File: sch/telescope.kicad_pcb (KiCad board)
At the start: 2 copper layers, 56.2 x 77 mm, 72 parts, among them J1 USB_B, J2 M1, J3 M2, J4 12V, J5 UART, Q1 MMBT3904, Q2 MMBT3904, Q3 MMBT3904, SW1 RST, SW2 IO0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

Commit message: fix feedback resistor value
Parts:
- removed REF**: Ade, Logo:Ade
- R25: value 33k2 -> 10k

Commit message: fix missing copper layer logo
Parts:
- added REF**: Ade, Logo:Ade, F.Cu at (224.5, 100.6)

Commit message: add series resistor to led bjt
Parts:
- added R16: 10k, Resistor_SMD:R_0805_2012Metric_Pad1.20x1.40mm_HandSolder, F.Cu at (225.9, 111.5)
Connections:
- Q1 pad 1: /LED -> Net-(Q1-B)
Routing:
- net Net-(Q1-B): track 0.00 -> 3.64 mm
- net /LED: track 24.7 -> 25.7 mm

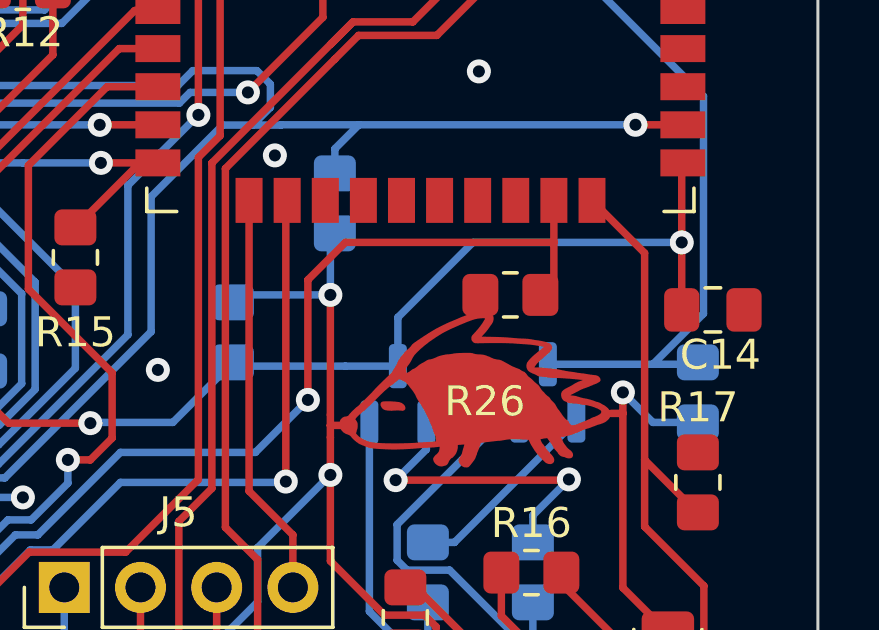
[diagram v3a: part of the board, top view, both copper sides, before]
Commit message: pull down bootstrap pin for serial logging
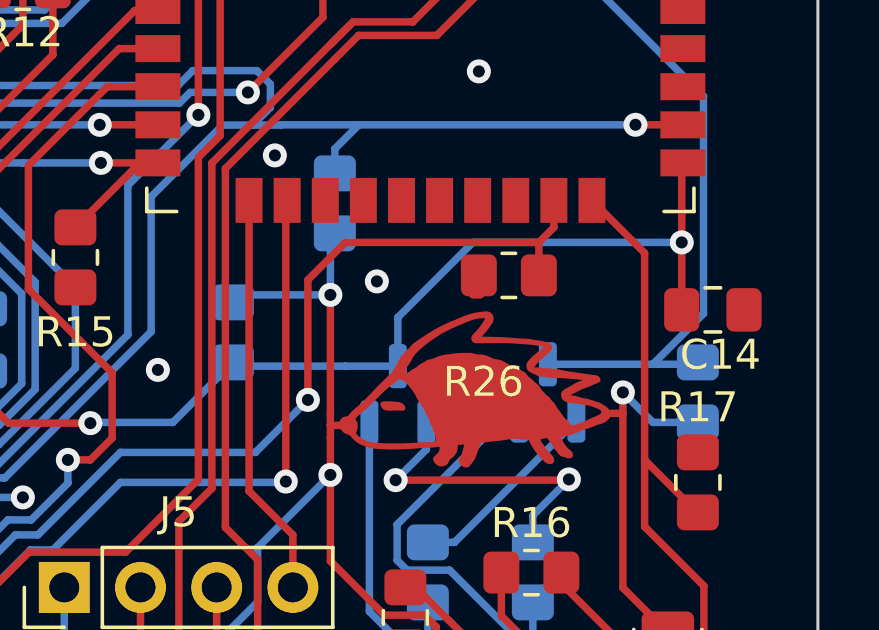
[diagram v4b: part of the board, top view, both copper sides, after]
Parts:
- C13: value 0.1uF -> 1uF
- moved R26 0.65 mm to (225.2, 101.6)
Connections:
- R26 pad 1: +3V3 -> GND
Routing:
- net /M2_STEP: track 35.6 -> 34.4 mm
- net GND: track 31.6 -> 31.9 mm, vias 29 -> 30
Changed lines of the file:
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@@
 	(footprint "Resistor_SMD:R_0805_2012Metric_Pad1.20x1.40mm_HandSolder"
 		(layer "F.Cu")
-		(at 225.25 102.25)
+		(at 225.2 101.6)
 		(descr "Resistor SMD 0805 (2012 Metric), square (rectangular) end terminal, IPC_7351 nominal with elongated pad for handsoldering. (Body size source: IPC-SM-782 page 72, https://www.pcb-3d.com/wordpress/wp-content/uploads/ipc-sm-782a_amendment_1_and_2.pdf), generated with kicad-footprint-generator")
 		(tags "resistor handsolder")
@@
 			(layers "F.Cu" "F.Paste" "F.Mask")
 			(roundrect_rratio 0.2083333333)
-			(net 9 "+3V3")
+			(net 2 "GND")
 			(pintype "passive")
 		)
@@
 			)
 		)
-		(property "Value" "0.1uF"
+		(property "Value" "1uF"
 			(at 0 -1.68 90)
 			(layer "B.Fab")
@@
 	)
 	(segment
+		(start 224.25 102.25)
+		(end 224 102.25)
+		(width 0.25)
+		(layer "F.Cu")
+		(net 2)
+	)
+	(segment
 		(start 217.775 123.449695)
 		(end 220.112348 121.112348)
@@
 	)
 	(via
+		(at 220.8 101.8)
+		(size 0.8)
+		(drill 0.4)
+		(layers "F.Cu" "B.Cu")
+		(free yes)
+		(net 2)
+	)
+	(via
 		(at 196.75 88)
 		(size 0.8)
@@
 	)
 	(segment
-		(start 224.25 102.25)
-		(end 224 102.25)
-		(width 0.25)
-		(layer "F.Cu")
-		(net 9)
-	)
-	(segment
 		(start 213.9929 127.24993)
 		(end 213.9929 125.949958)
@@
 	)
 	(segment
-		(start 226.7 100.5)
-		(end 226.7 101.8)
+		(start 226.2 100.5)
+		(end 219.75 100.5)
 		(width 0.25)
 		(layer "F.Cu")
@@
 	)
 	(segment
-		(start 226.7 99.1)
-		(end 226.7 100.5)
+		(start 226.2 101.6)
+		(end 226.2 100.5)
 		(width 0.25)
 		(layer "F.Cu")
@@
 	)
 	(segment
-		(start 226.7 100.5)
-		(end 219.75 100.5)
+		(start 226.7 100)
+		(end 226.2 100.5)
 		(width 0.25)
 		(layer "F.Cu")
@@
 	)
 	(segment
-		(start 226.7 101.8)
-		(end 226.25 102.25)
+		(start 226.7 99.1)
+		(end 226.7 100)
 		(width 0.25)
 		(layer "F.Cu")

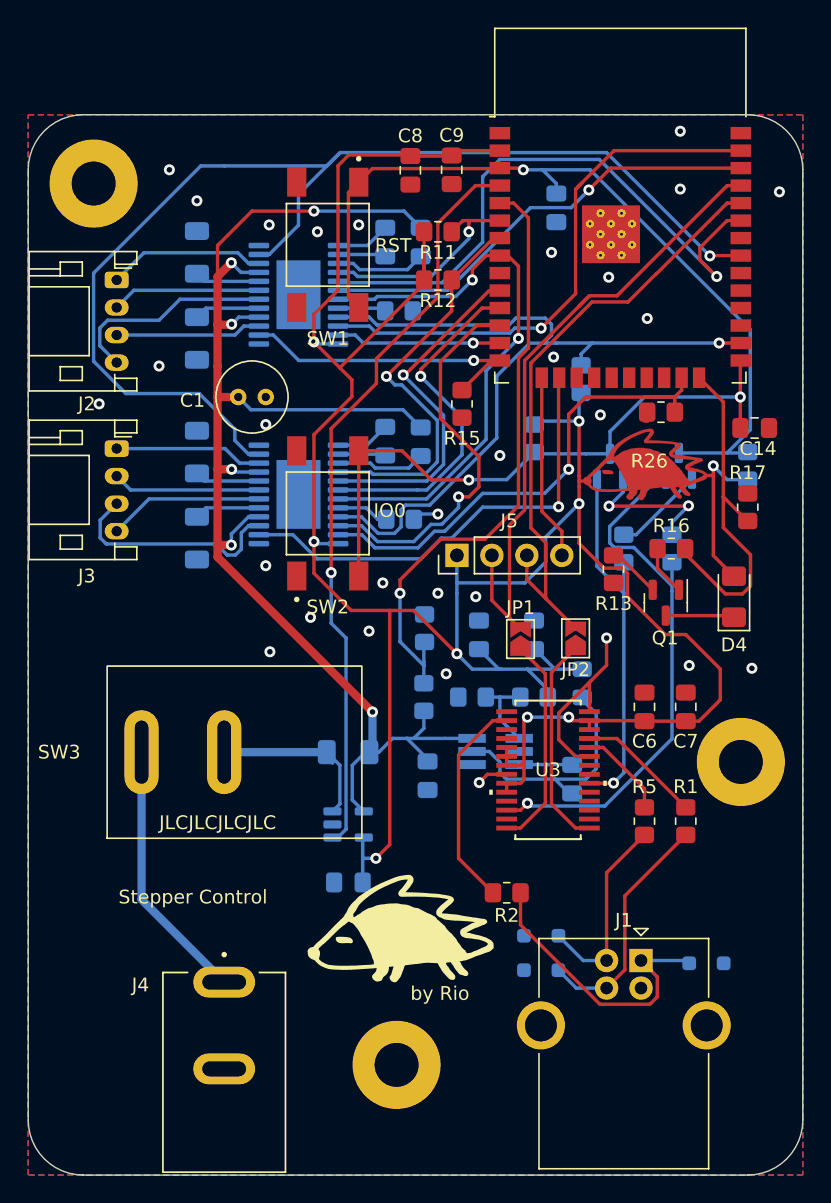
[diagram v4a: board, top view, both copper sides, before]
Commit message: split motor driver enable lines and increase motor trace width
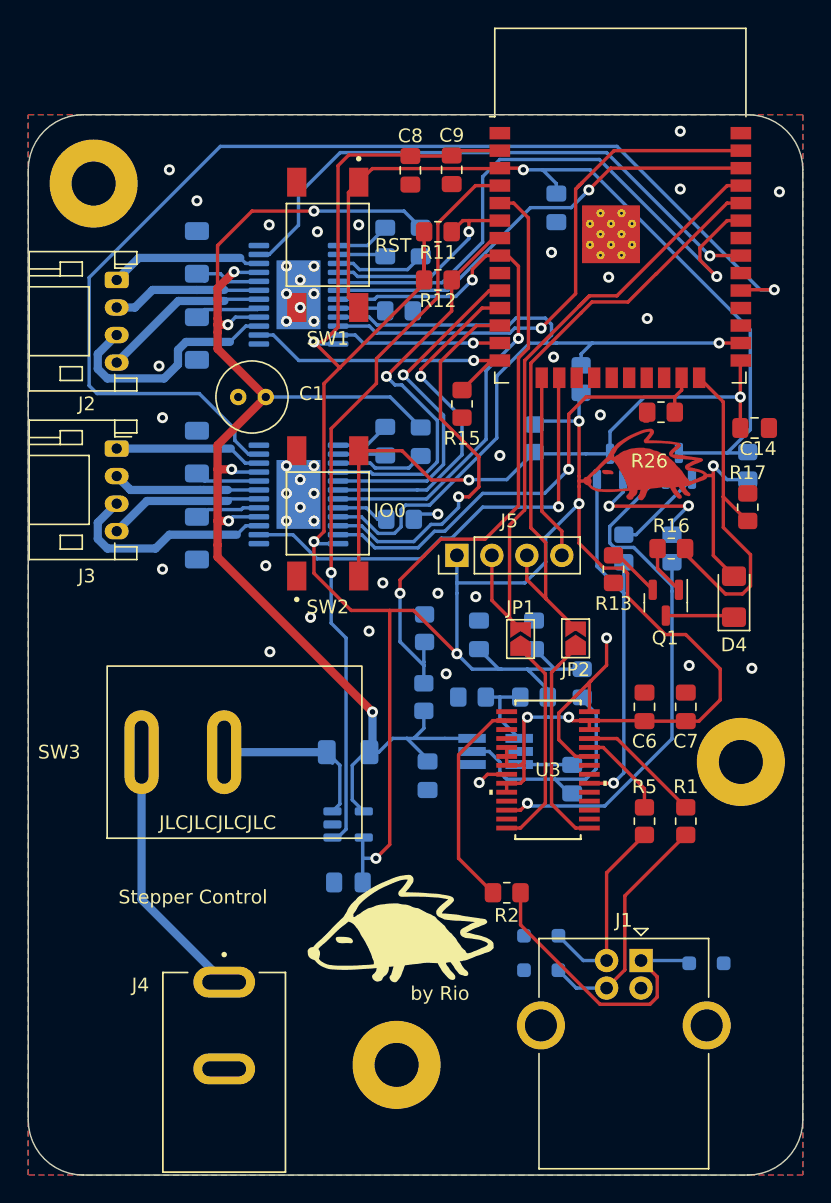
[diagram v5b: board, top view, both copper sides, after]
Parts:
- moved C1 2.00 mm to (196.5, 100.5), turned to 180 degrees
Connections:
- U1 pad 23: /~{M_ENA} -> /~{M1_ENA}
- U2 pad 23: /~{M_ENA} -> /~{M2_ENA}
- U5 pad 29: unconnected-(U5-IO5-Pad29) -> /~{M2_ENA}
- U5 pad 31: /~{M_ENA} -> /~{M1_ENA}
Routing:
- net /~{M_ENA}: track 85.7 -> 0.00 mm, vias 1 -> 0
- net /~{M2_ENA}: track 0.00 -> 83.2 mm, vias 0 -> 1
- net /~{M1_ENA}: track 0.00 -> 42.5 mm, vias 0 -> 1
- net Net-(J2-Pin_3): track 10.6 -> 17.2 mm
- net Net-(J2-Pin_4): track 15.4 -> 12.2 mm
- net +12V: track 106.1 -> 104.1 mm
- net Net-(U1-SENSE2): track 4.73 -> 5.53 mm
- net Net-(J3-Pin_3): track 16.6 -> 15.8 mm
- net GND: vias 30 -> 46

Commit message: update pcb
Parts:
- added D5: PDZ3.6B, Diode_SMD:D_SOD-323_HandSoldering, B.Cu at (219.2, 116.8)
- added D6: CUS10S30, Diode_SMD:D_SOD-323_HandSoldering, F.Cu at (195.2, 139.0)
- added J6: Conn_01x02, Connector_PinHeader_2.54mm:PinHeader_1x02_P2.54mm_Vertical, F.Cu at (207.5, 121.0)
- added JP3: SolderJumper_2_Open, Jumper:SolderJumper-2_P1.3mm_Open_TrianglePad1.0x1.5mm, B.Cu at (203.7, 122.8)
- added JP4: SolderJumper_2_Open, Jumper:SolderJumper-2_P1.3mm_Open_TrianglePad1.0x1.5mm, B.Cu at (203.7, 120.2)
- added Q4: MMBT3904, Package_TO_SOT_SMD:SOT-23, B.Cu at (197.0, 121.0)
- added R27: DNP, Resistor_SMD:R_0805_2012Metric_Pad1.20x1.40mm_HandSolder, F.Cu at (227.4, 101.6)
- added R30: 10k, Resistor_SMD:R_0805_2012Metric_Pad1.20x1.40mm_HandSolder, B.Cu at (198.0, 124.2)
- added RV1: R_Potentiometer_US, Potentiometer_SMD:Potentiometer_Bourns_TC33X_Vertical, B.Cu at (191.0, 118.2)
- added TP1: TestPoint, TestPoint:TestPoint_Pad_D1.5mm, B.Cu at (185.2, 118.2)
- moved R22 9.58 mm to (202.4, 114.5), turned to 180 degrees
- moved R21 5.63 mm to (202.4, 117.2), turned to 0 degrees
- moved R2 4.61 mm to (210.5, 133.5), turned to 90 degrees
- moved R26 1.60 mm to (223.6, 101.6)
- moved C13 1.10 mm to (216.5, 86.8)
- turned C8 to 90 degrees
- turned C9 to 90 degrees
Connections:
- U1 pad 12: +3V3 -> Net-(U1-VREF)
- U2 pad 12: +3V3 -> Net-(U1-VREF)
- U5 pad 27: /GPS_TX -> /GPO
- U5 pad 28: /GPS_RX -> unconnected-(U5-IO17-Pad28)
- U5 pad 30: /GPS_FIX -> unconnected-(U5-IO18-Pad30)
- U5 pad 9: /~{GPS_RST} -> unconnected-(U5-IO33-Pad9)
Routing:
- net /GPO: track 0.00 -> 70.7 mm, vias 0 -> 3
- net Net-(U1-VREF): track 0.00 -> 39.7 mm, vias 0 -> 3
- net VBUS: track 21.6 -> 56.9 mm
- net Net-(J6-Pin_2): track 0.00 -> 10.6 mm, vias 0 -> 1
- net +12V: track 104.1 -> 114.3 mm, vias 6 -> 7
- net /ISENSE: track 54.5 -> 64.7 mm
- net +3V3: track 203.2 -> 212.9 mm
- net Net-(J6-Pin_1): track 0.00 -> 5.42 mm
- net Net-(U3-VBUS_DET): track 15.6 -> 10.5 mm
- net /ESP_EN: track 60.2 -> 65.1 mm, vias 1 -> 3
- net Net-(D6-K): track 19.2 -> 23.4 mm
- net /~{M2_ENA}: track 83.2 -> 86.3 mm
- net /~{M1_ENA}: track 42.5 -> 45.6 mm
- net Net-(Q4-B): track 0.00 -> 2.69 mm
- net GND: track 31.9 -> 34.1 mm, vias 46 -> 49
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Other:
- board text added: "Stepper Control v2"
- board text removed: "JLCJLCJLCJLC"
- board text removed: "Stepper Control"

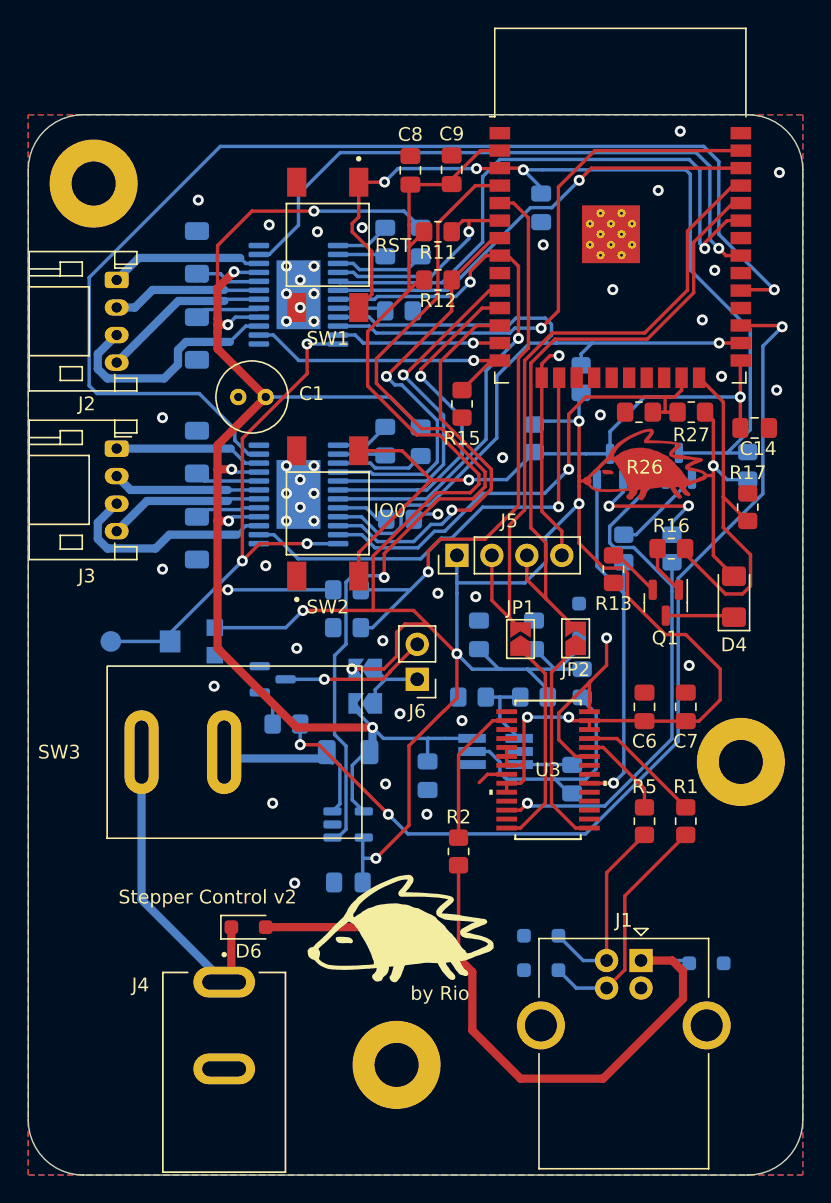
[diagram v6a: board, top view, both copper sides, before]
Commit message: switch to jst and generate v2 gerbers
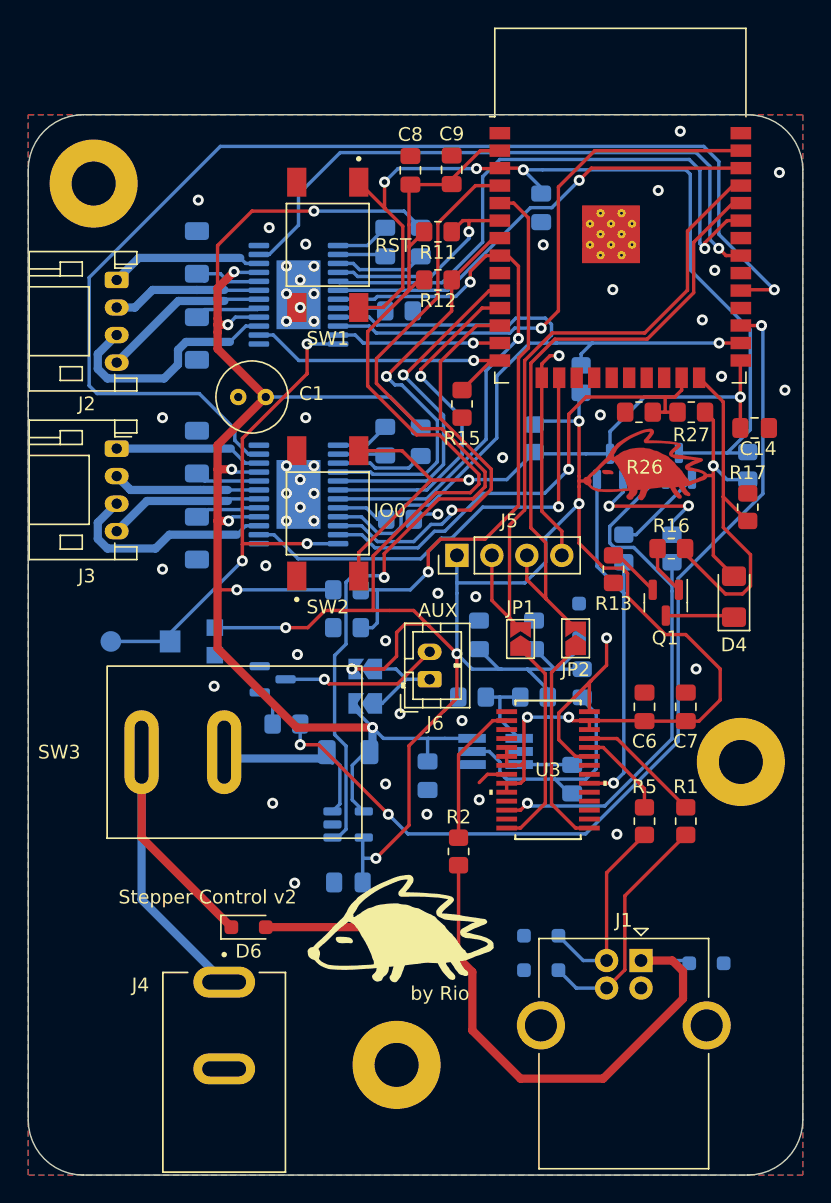
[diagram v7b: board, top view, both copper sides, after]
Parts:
- J6: value Conn_01x02 -> AUX; footprint Connector_PinHeader_2.54mm:PinHeader_1x02_P2.54mm_Vertical -> Connector_JST:JST_PH_B2B-PH-K_1x02_P2.00mm_Vertical
- moved J6 0.90 mm to (208.4, 121.0), turned to 90 degrees
- renumbered R30 to R28
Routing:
- net Net-(D6-K): track 23.4 -> 35.3 mm
- net /ESP_EN: track 65.1 -> 67.7 mm
- net /GPO: track 70.7 -> 68.7 mm
- net Net-(J6-Pin_1): track 5.42 -> 7.24 mm
- net /VSENSE: track 43.3 -> 42.3 mm
- net Net-(J6-Pin_2): track 10.6 -> 11.6 mm
- net GND: vias 49 -> 51
